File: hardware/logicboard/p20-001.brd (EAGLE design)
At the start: 72 x 72 mm, 28 parts, among them IC11 74ALS04N, J0 DC9V, J11 AUDIO_JACK_3.5MM_PTH, J12 AUDIO_JACK_3.5MM_PTH, J13 AUDIO_JACK_3.5MM_PTH, J14 AUDIO_JACK_3.5MM_PTH, J7 DIN5, J8 DIN5, J9 DIN5, X0 MKDSN1,5/2-5,08

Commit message: Renumbered signals and parts.
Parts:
- renumbered L0 to L00, L1/2 to L0/1
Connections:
- net LED2 renamed LED0
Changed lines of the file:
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@@
 <attribute name="VALUE" x="46.8664" y="44.6886" size="0.9906" layer="27" ratio="10"/>
 </element>
-<element name="L0" library="led" library_urn="urn:adsk.eagle:library:259" package="LED3MM" package3d_urn="urn:adsk.eagle:package:15797/1" value="PWR" x="3" y="55" smashed="yes" rot="R90">
+<element name="L00" library="led" library_urn="urn:adsk.eagle:library:259" package="LED3MM" package3d_urn="urn:adsk.eagle:package:15797/1" value="PWR" x="3" y="55" smashed="yes" rot="R90">
 <attribute name="NAME" x="3" y="57.5" size="1" layer="25" ratio="10" rot="R180" align="center"/>
 <attribute name="POPULARITY" value="97" x="3" y="55" size="1.778" layer="27" rot="R90" display="off"/>
@@
 <attribute name="VALUE" x="6.175" y="6.19" size="1.27" layer="27" rot="R90"/>
 </element>
-<element name="L1/2" library="led" library_urn="urn:adsk.eagle:library:259" package="DUOLED-C-5MM" package3d_urn="urn:adsk.eagle:package:15851/1" value="" x="3" y="62" smashed="yes" rot="R270">
+<element name="L0/1" library="led" library_urn="urn:adsk.eagle:library:259" package="DUOLED-C-5MM" package3d_urn="urn:adsk.eagle:package:15851/1" value="" x="3" y="62" smashed="yes" rot="R270">
 <attribute name="NAME" x="3" y="66" size="1" layer="25" ratio="10" align="center"/>
 <attribute name="POPULARITY" value="1" x="3" y="62" size="1.778" layer="27" rot="R270" display="off"/>
@@
 <contactref element="J13" pad="SLEEVE"/>
 <contactref element="J14" pad="SLEEVE"/>
-<contactref element="L0" pad="K"/>
+<contactref element="L00" pad="K"/>
 <contactref element="IC11" pad="7"/>
 <contactref element="X0" pad="1"/>
 <contactref element="S1" pad="1"/>
 <contactref element="S1" pad="2"/>
-<contactref element="L1/2" pad="C"/>
+<contactref element="L0/1" pad="C"/>
 <contactref element="JP6" pad="2"/>
 <contactref element="SV2" pad="11"/>
@@
 <signal name="LEDPWR">
 <contactref element="R10" pad="1"/>
-<contactref element="L0" pad="A"/>
+<contactref element="L00" pad="A"/>
 <wire x1="3" y1="53.73" x2="20.46" y2="44" width="0" layer="19" extent="1-1"/>
 </signal>
@@
 <wire x1="6.54" y1="-4" x2="3" y2="7.46" width="0" layer="19" extent="1-1"/>
 </signal>
-<signal name="LED2">
+<signal name="LED0">
 <contactref element="JP6" pad="3"/>
 <contactref element="SV2" pad="17"/>
@@
 </signal>
 <signal name="N$3">
-<contactref element="L1/2" pad="AR"/>
+<contactref element="L0/1" pad="AR"/>
 <contactref element="R11" pad="1"/>
 <wire x1="1.46" y1="-4" x2="3" y2="59.46" width="0" layer="19" extent="1-1"/>
 </signal>
 <signal name="N$5">
-<contactref element="L1/2" pad="AX"/>
+<contactref element="L0/1" pad="AX"/>
 <contactref element="R12" pad="2"/>
 <wire x1="6.54" y1="-8" x2="3" y2="64.54" width="0" layer="19" extent="1-1"/>

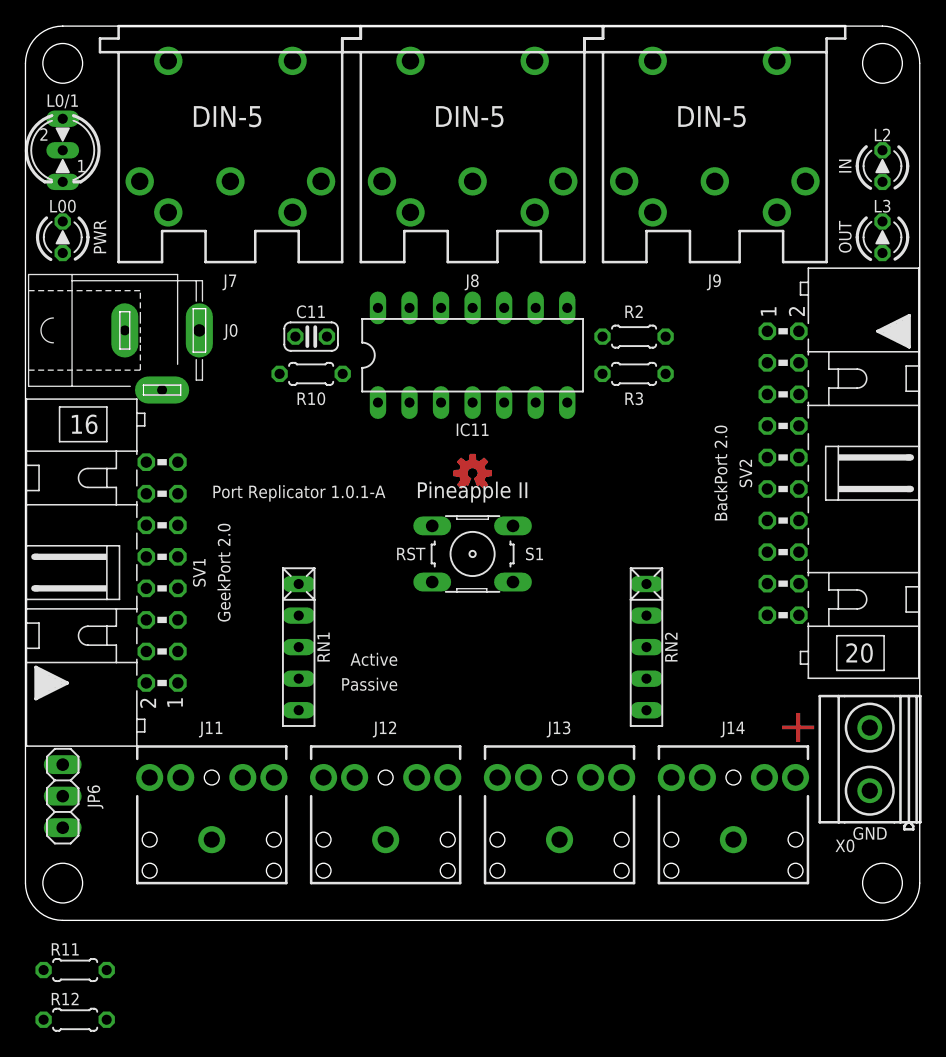
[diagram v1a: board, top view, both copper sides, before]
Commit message: Renumbered parts.
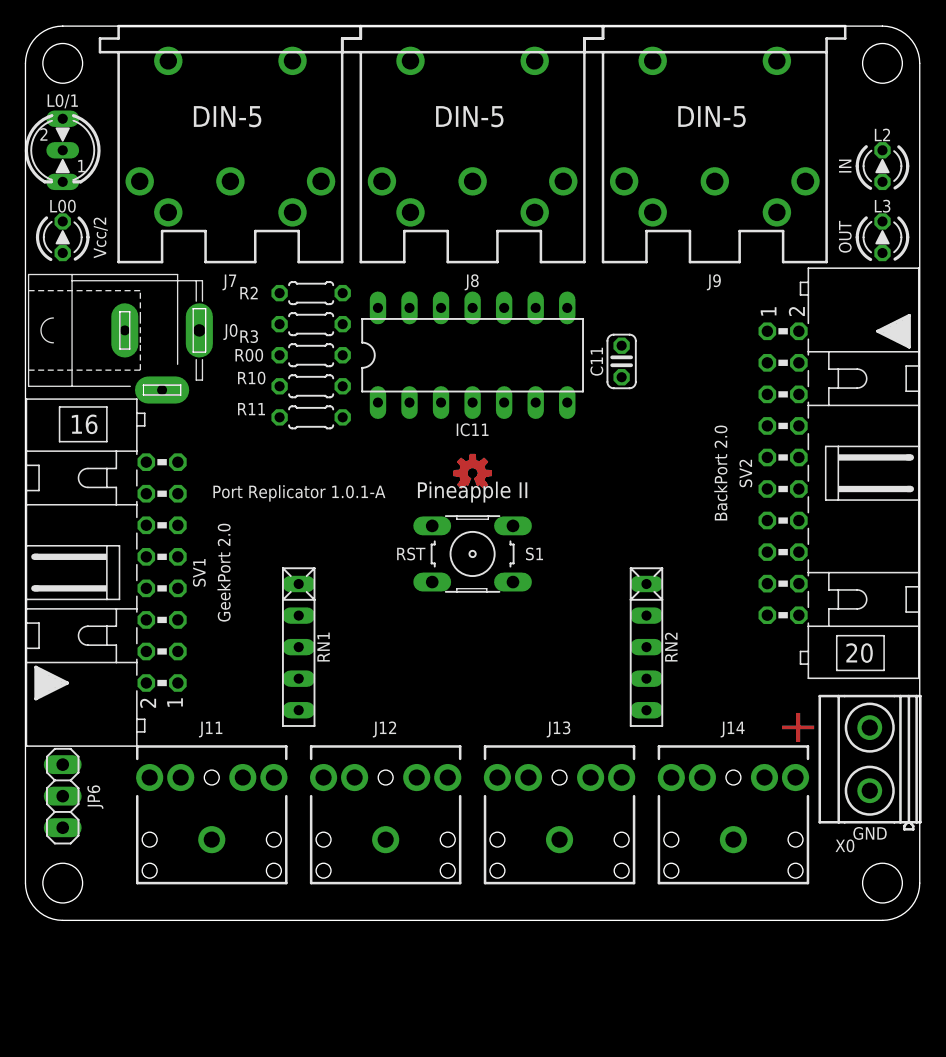
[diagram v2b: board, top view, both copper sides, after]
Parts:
- removed R12: (no value), rcl:0204/5
- added R00: (no value), rcl:0204/5
- moved R11 48.4 mm to (23.0, 40.5)
- moved R3 26.3 mm to (23.0, 48.0)
- moved R2 26.2 mm to (23.0, 50.5)
- moved C11 25.1 mm to (48.0, 45.0), turned to 90 degrees
- moved R10 1.00 mm to (23.0, 43.0)
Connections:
- net LED0: now also R11.1; no longer R12.1
- net LED1: now also R10.2; no longer R11.2
- net LEDPWR: now also R00.1; no longer R10.1
- net N$3: now also R10.1; no longer R11.1
- net N$5: now also R11.2; no longer R12.2
- net VCC/2: now also R00.2; no longer R10.2
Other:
- board text added: "Vcc/2"
- board text removed: "Active"
- board text removed: "PWR"
- board text removed: "Passive"

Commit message: Adopted to GeekPort II and BackPort II.
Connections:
- removed net ANLG4R: J14.RING, SV1.16
- removed net DTCT4: J14.TSH, RN1.5, SV1.15
- new net ANLG0R: J11.RING, SV1.3
- new net DTCT0: J11.TSH, RN1.2, SV1.2
- net ANLG1R: now also J12.RING, SV1.7; no longer J11.RING, SV1.4
- net ANLG2R: now also J13.RING, SV1.11; no longer J12.RING, SV1.8
- net ANLG3R: now also J14.RING, SV1.15; no longer J13.RING, SV1.12
- net DTCT1: now also J12.TSH, RN1.3, SV1.6; no longer J11.TSH, RN1.2, SV1.3
- net DTCT2: now also J13.TSH, RN1.4, SV1.10; no longer J12.TSH, RN1.3, SV1.7
- net DTCT3: now also J14.TSH, RN1.5, SV1.14; no longer J13.TSH, RN1.4, SV1.11
- net GND: now also SV2.15, SV2.16, SV2.5; no longer SV2.10, SV2.11, SV2.13
- net LED0: now also SV2.7; no longer SV2.17
- net LED1: now also SV2.20; no longer SV2.9
- net MIRTN: now also SV2.11; no longer SV2.5
- net MISND: now also SV2.9; no longer SV2.4
- net MORTN: now also SV2.17; no longer SV2.15
- net MOSND: now also SV2.13; no longer SV2.14
- net MRXDTCT: now also SV2.4; no longer SV2.7
- net MTRTN: now also SV2.18; no longer SV2.20
- net MTSND: now also SV2.14; no longer SV2.19
- net MTX+: now also SV2.10; no longer SV2.16
- net MTX-: now also SV2.12; no longer SV2.18
- net VCC: now also SV2.19; no longer SV2.12
- net VCC/2: now also SV1.12, SV1.16, SV1.4, SV1.8; no longer SV1.10, SV1.14, SV1.2, SV1.6

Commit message: Renamed signals.
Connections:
- net N$3 renamed LED1A
- net N$5 renamed LED0A
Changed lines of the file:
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@@
 <hole x="69" y="69" drill="3.2"/>
 <hole x="3" y="69" drill="3.2"/>
-<circle x="3" y="3" radius="2.236065625" width="0.2" layer="42"/>
-<circle x="69" y="3" radius="2.236065625" width="0.2" layer="42"/>
-<circle x="69" y="69" radius="2.236065625" width="0.2" layer="42"/>
-<circle x="3" y="69" radius="2.236065625" width="0.2" layer="42"/>
-<circle x="3" y="69" radius="2.236065625" width="0.2" layer="41"/>
-<circle x="69" y="69" radius="2.236065625" width="0.2" layer="41"/>
-<circle x="3" y="3" radius="2.236065625" width="0.2" layer="41"/>
-<circle x="69" y="3" radius="2.236065625" width="0.2" layer="41"/>
+<circle x="3" y="3" radius="2.25" width="0.2" layer="42"/>
+<circle x="69" y="3" radius="2.25" width="0.2" layer="42"/>
+<circle x="69" y="69" radius="2.25" width="0.2" layer="42"/>
+<circle x="3" y="69" radius="2.25" width="0.2" layer="42"/>
+<circle x="3" y="69" radius="2.25" width="0.2" layer="41"/>
+<circle x="69" y="69" radius="2.25" width="0.2" layer="41"/>
+<circle x="3" y="3" radius="2.25" width="0.2" layer="41"/>
+<circle x="69" y="3" radius="2.25" width="0.2" layer="41"/>
 <polygon width="0.2" layer="43">
 <vertex x="42" y="38"/>
@@
 <text x="36" y="34" size="1.27" layer="25" align="bottom-center">Pineapple II</text>
 <wire x1="0" y1="69" x2="0" y2="3" width="0" layer="20"/>
-<circle x="44" y="69" radius="2.236065625" width="0.2" layer="41"/>
-<circle x="44" y="3" radius="2.236065625" width="0.2" layer="41"/>
 <text x="22" y="34.5" size="1" layer="25" align="center">Port Replicator 1.0.1-A</text>
 <wire x1="72" y1="3" x2="72" y2="69" width="0" layer="20"/>
@@
 <contactref element="SV2" pad="12"/>
 </signal>
-<signal name="N$3">
+<signal name="LED1A">
 <contactref element="L0/1" pad="AR"/>
 <contactref element="R10" pad="1"/>
 <wire x1="20.46" y1="43" x2="3" y2="59.46" width="0" layer="19" extent="1-1"/>
 </signal>
-<signal name="N$5">
+<signal name="LED0A">
 <contactref element="L0/1" pad="AX"/>
 <contactref element="R11" pad="2"/>
